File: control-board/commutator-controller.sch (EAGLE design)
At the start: 39 parts, among them U1 PTN04050C, U2 LTC4425EMSE#PBF, U3 IS31FL3193, U4 TMC2130, U5 TEENSY-3.2

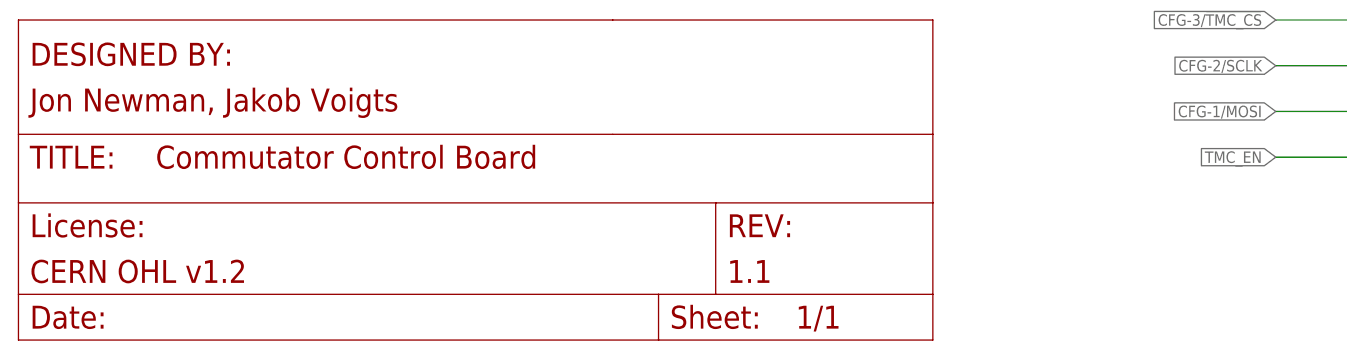
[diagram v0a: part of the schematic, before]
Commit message: Small changes to the commutator driver board
- No change in BOM or functionality
- Added silkscreen outline to LED touch pad
- Added OE logo
- Remove license from silkscreen
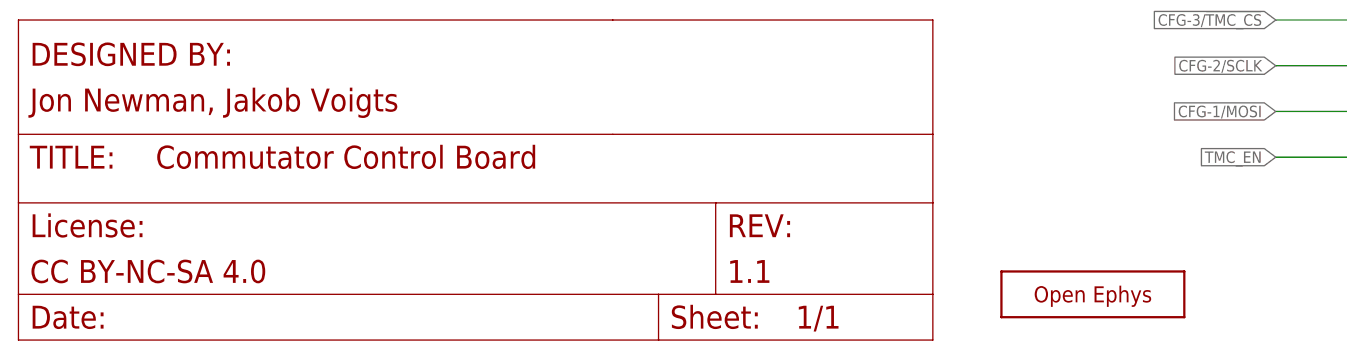
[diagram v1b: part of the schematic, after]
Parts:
- added X1: OE-LOGO_7X5, jonnew:OE-LOGO_7X5
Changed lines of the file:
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@@
 <attribute name="DESIGNER" value="Jon Newman, Jakob Voigts"/>
 <attribute name="DESIGN_NAME" value="Commutator Control Board"/>
-<attribute name="LICENSE" value="CERN OHL v1.2"/>
+<attribute name="LICENSE" value="CC BY-NC-SA 4.0"/>
 <attribute name="REVISION" value="1.1"/>
 </attributes>
@@
 <part name="U$4" library="jonnew" deviceset="VCC" device=""/>
 <part name="SUPPLY1" library="jonnew" deviceset="GND" device=""/>
+<part name="X1" library="jonnew" deviceset="OE-LOGO" device="_7X5"/>
 </parts>
 <sheets>
@@
 <instance part="U$4" gate="VCC" x="149.86" y="246.38"/>
 <instance part="SUPPLY1" gate="PE" x="93.98" y="198.12"/>
+<instance part="X1" gate="G$1" x="127" y="12.7"/>
 </instances>
 <busses>
